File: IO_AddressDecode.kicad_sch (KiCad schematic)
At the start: 43 parts, among them J0 Cassette Data In, J13 74LS74, J14 GAME_IO_Conn, J2 Cassette Data Out, J3 Conn_01x16, K13 MA741, Q4 MPSA13

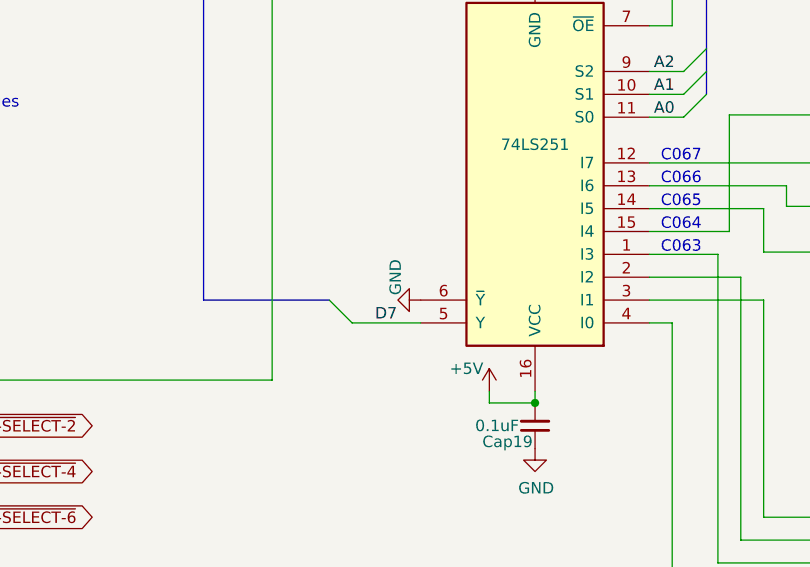
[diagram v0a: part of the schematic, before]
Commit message: fix H14 pin 6
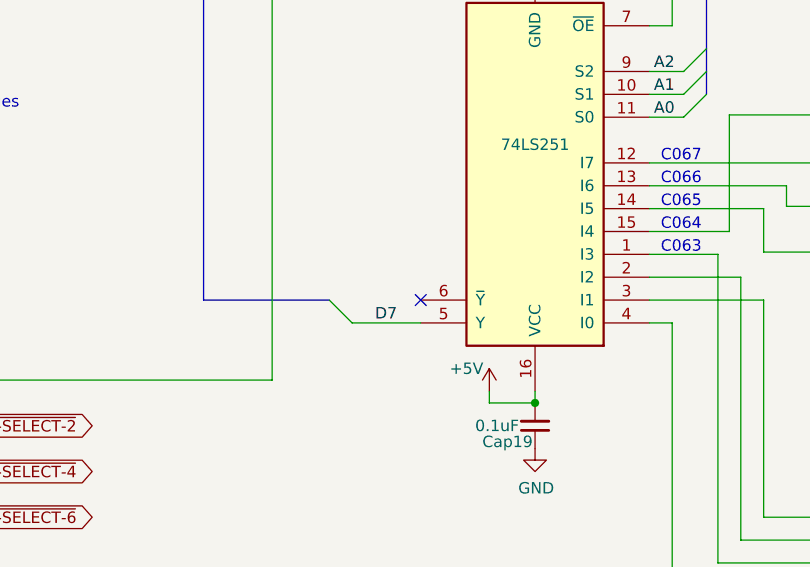
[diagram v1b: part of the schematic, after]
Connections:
- net GND: no longer H14.6 (~{Y})
- no-connect marks 11 -> 12
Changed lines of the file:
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@@
   (no_connect (at 240.03 198.12))
   (no_connect (at 194.31 187.96))
+  (no_connect (at 156.21 106.68))
   (no_connect (at 194.31 185.42))
   (no_connect (at 316.23 241.3))
@@
         )
       )
-    )
-  )
-  (symbol (lib_id "power:GND") (at 156.21 106.68 270) (unit 1)
-    (in_bom yes) (on_board yes) (dnp no)
-    (property "Reference" "#PWR012" (at 149.86 106.68 0)
-      (effects (font (size 1.27 1.27)) hide)
-    )
-    (property "Value" "GND" (at 153.416 104.14 0)
-      (effects (font (size 1.27 1.27)))
-    )
-    (property "Footprint" "" (at 156.21 106.68 0)
-      (effects (font (size 1.27 1.27)) hide)
-    )
-    (property "Datasheet" "" (at 156.21 106.68 0)
-      (effects (font (size 1.27 1.27)) hide)
-    )
-    (pin "1")
-    (instances
-      (project "AppleII"
-        (path "/f1f08369-4db3-46f7-9b89-a5d3cfbed55a/00000000-0000-0000-0000-00006017a131"
-          (reference "#PWR012") (unit 1)
-        )
-      )

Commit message: add missing test points
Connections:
- net KBD_Data0 renamed KBD0
- net KBD_Data1 renamed KBD1
- net KBD_Data2 renamed KBD2
- net KBD_Data3 renamed KBD3
- net KBD_Data4 renamed KBD4
- net KBD_Data5 renamed KBD5
- net KBD_Data6 renamed KBD6
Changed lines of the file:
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@@
     (effects (font (size 1.27 1.27)) (justify left bottom))
   )
-  (label "KBD_Data6" (at 195.58 182.88 0) (fields_autoplaced)
+  (label "KBD6" (at 195.58 182.88 0) (fields_autoplaced)
     (effects (font (size 1.27 1.27)) (justify left bottom))
   )
@@
     (effects (font (size 1.27 1.27)) (justify left bottom))
   )
-  (label "KBD_Data1" (at 273.05 170.18 180) (fields_autoplaced)
+  (label "KBD1" (at 273.05 170.18 180) (fields_autoplaced)
     (effects (font (size 1.27 1.27)) (justify right bottom))
   )
@@
     (effects (font (size 1.27 1.27)) (justify left bottom))
   )
-  (label "KBD_Data0" (at 195.58 162.56 0) (fields_autoplaced)
+  (label "KBD0" (at 195.58 162.56 0) (fields_autoplaced)
     (effects (font (size 1.27 1.27)) (justify left bottom))
   )
@@
     (effects (font (size 1.27 1.27)) (justify left bottom))
   )
-  (label "KBD_Data6" (at 226.314 177.8 0) (fields_autoplaced)
-    (effects (font (size 1.27 1.27)) (justify left bottom))
-  )
-  (label "KBD_Data2" (at 195.58 167.64 0) (fields_autoplaced)
+  (label "KBD6" (at 226.314 177.8 0) (fields_autoplaced)
+    (effects (font (size 1.27 1.27)) (justify left bottom))
+  )
+  (label "KBD2" (at 195.58 167.64 0) (fields_autoplaced)
     (effects (font (size 1.27 1.27)) (justify left bottom))
   )
@@
     (effects (font (size 1.27 1.27)) (justify left bottom))
   )
-  (label "KBD_Data4" (at 195.58 180.34 0) (fields_autoplaced)
+  (label "KBD4" (at 195.58 180.34 0) (fields_autoplaced)
     (effects (font (size 1.27 1.27)) (justify left bottom))
   )
@@
     (effects (font (size 1.27 1.27)) (justify left bottom))
   )
-  (label "KBD_Data5" (at 195.58 177.8 0) (fields_autoplaced)
+  (label "KBD5" (at 195.58 177.8 0) (fields_autoplaced)
     (effects (font (size 1.27 1.27)) (justify left bottom))
   )
@@
     (effects (font (size 1.27 1.27)) (justify left bottom))
   )
-  (label "KBD_Data3" (at 273.05 175.26 180) (fields_autoplaced)
-    (effects (font (size 1.27 1.27)) (justify right bottom))
-  )
-  (label "KBD_Data1" (at 195.58 154.94 0) (fields_autoplaced)
-    (effects (font (size 1.27 1.27)) (justify left bottom))
-  )
-  (label "KBD_Data3" (at 195.58 165.1 0) (fields_autoplaced)
-    (effects (font (size 1.27 1.27)) (justify left bottom))
-  )
-  (label "KBD_Data5" (at 226.314 172.72 0) (fields_autoplaced)
+  (label "KBD3" (at 273.05 175.26 180) (fields_autoplaced)
+    (effects (font (size 1.27 1.27)) (justify right bottom))
+  )
+  (label "KBD1" (at 195.58 154.94 0) (fields_autoplaced)
+    (effects (font (size 1.27 1.27)) (justify left bottom))
+  )
+  (label "KBD3" (at 195.58 165.1 0) (fields_autoplaced)
+    (effects (font (size 1.27 1.27)) (justify left bottom))
+  )
+  (label "KBD5" (at 226.314 172.72 0) (fields_autoplaced)
     (effects (font (size 1.27 1.27)) (justify left bottom))
   )
@@
     (effects (font (size 1.27 1.27)) (justify left bottom))
   )
-  (label "KBD_Data2" (at 273.05 177.8 180) (fields_autoplaced)
+  (label "KBD2" (at 273.05 177.8 180) (fields_autoplaced)
     (effects (font (size 1.27 1.27)) (justify right bottom))
   )
@@
     (effects (font (size 1.27 1.27)) (justify left bottom))
   )
-  (label "KBD_Data0" (at 273.05 172.72 180) (fields_autoplaced)
+  (label "KBD0" (at 273.05 172.72 180) (fields_autoplaced)
     (effects (font (size 1.27 1.27)) (justify right bottom))
   )
@@
     (effects (font (size 1.27 1.27)) (justify left bottom))
   )
-  (label "KBD_Data4" (at 226.314 175.26 0) (fields_autoplaced)
+  (label "KBD4" (at 226.314 175.26 0) (fields_autoplaced)
     (effects (font (size 1.27 1.27)) (justify left bottom))
   )
@@
     (effects (font (size 1.27 1.27)) (justify right))
   )
-  (hierarchical_label "KBD_Data[0..6]" (shape output) (at 223.52 148.59 90) (fields_autoplaced)
-    (effects (font (size 1.27 1.27)) (justify left))
-  )
+  (hierarchical_label "KBD[0..6]" (shape output) (at 223.52 148.59 90) (fields_autoplaced)
+    (effects (font (size 1.27 1.27)) (justify left))
+  )
